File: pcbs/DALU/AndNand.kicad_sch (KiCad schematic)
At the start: 6 parts, among them U501 74HC00, U502 74HC00, U503 74HC14, U504 74HC14, U505 74HC245, U506 74HC245

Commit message: More routing
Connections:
- net A2: now also U501.9; no longer U501.12
- net A3: now also U501.12; no longer U501.9
- net A6: now also U502.9; no longer U502.12
- net A7: now also U502.12; no longer U502.9
- net B2: now also U501.10; no longer U501.13
- net B3: now also U501.13; no longer U501.10
- net B6: now also U502.10; no longer U502.13
- net B7: now also U502.13; no longer U502.10
- net NAND2: now also U501.8; no longer U501.11
- net NAND3: now also U501.11; no longer U501.8
- net NAND6: now also U502.8; no longer U502.11
- net NAND7: now also U502.11; no longer U502.8
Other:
- moved on the sheet: U501C, U501D, U502C, U502D
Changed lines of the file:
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@@
     (pin "7")
   )
-  (symbol (lib_id "74xx:74HC00") (at 83.82 71.12 0) (unit 4)
-    (in_bom yes) (on_board yes) (fields_autoplaced)
-    (property "Reference" "U501" (id 0) (at 83.82 62.23 0))
-    (property "Value" "74HC00" (id 1) (at 83.82 64.77 0))
-    (property "Footprint" "Package_DIP:DIP-14_W7.62mm_Socket" (id 2) (at 83.82 71.12 0)
-      (effects (font (size 1.27 1.27)) hide)
-    )
-    (property "Datasheet" "http://www.ti.com/lit/gpn/sn74hc00" (id 3) (at 83.82 71.12 0)
+  (symbol (lib_id "74xx:74HC00") (at 83.82 85.09 0) (unit 4)
+    (in_bom yes) (on_board yes) (fields_autoplaced)
+    (property "Reference" "U501" (id 0) (at 83.82 76.2 0))
+    (property "Value" "74HC00" (id 1) (at 83.82 78.74 0))
+    (property "Footprint" "Package_DIP:DIP-14_W7.62mm_Socket" (id 2) (at 83.82 85.09 0)
+      (effects (font (size 1.27 1.27)) hide)
+    )
+    (property "Datasheet" "http://www.ti.com/lit/gpn/sn74hc00" (id 3) (at 83.82 85.09 0)
       (effects (font (size 1.27 1.27)) hide)
     )
@@
     (pin "1")
   )
-  (symbol (lib_id "74xx:74HC00") (at 83.82 140.97 0) (unit 3)
-    (in_bom yes) (on_board yes) (fields_autoplaced)
-    (property "Reference" "U502" (id 0) (at 83.82 132.08 0))
-    (property "Value" "74HC00" (id 1) (at 83.82 134.62 0))
-    (property "Footprint" "Package_DIP:DIP-14_W7.62mm_Socket" (id 2) (at 83.82 140.97 0)
-      (effects (font (size 1.27 1.27)) hide)
-    )
-    (property "Datasheet" "http://www.ti.com/lit/gpn/sn74hc00" (id 3) (at 83.82 140.97 0)
+  (symbol (lib_id "74xx:74HC00") (at 83.82 127 0) (unit 3)
+    (in_bom yes) (on_board yes) (fields_autoplaced)
+    (property "Reference" "U502" (id 0) (at 83.82 118.11 0))
+    (property "Value" "74HC00" (id 1) (at 83.82 120.65 0))
+    (property "Footprint" "Package_DIP:DIP-14_W7.62mm_Socket" (id 2) (at 83.82 127 0)
+      (effects (font (size 1.27 1.27)) hide)
+    )
+    (property "Datasheet" "http://www.ti.com/lit/gpn/sn74hc00" (id 3) (at 83.82 127 0)
       (effects (font (size 1.27 1.27)) hide)
     )
@@
     (pin "1")
   )
-  (symbol (lib_id "74xx:74HC00") (at 83.82 85.09 0) (unit 3)
-    (in_bom yes) (on_board yes) (fields_autoplaced)
-    (property "Reference" "U501" (id 0) (at 83.82 76.2 0))
-    (property "Value" "74HC00" (id 1) (at 83.82 78.74 0))
-    (property "Footprint" "Package_DIP:DIP-14_W7.62mm_Socket" (id 2) (at 83.82 85.09 0)
-      (effects (font (size 1.27 1.27)) hide)
-    )
-    (property "Datasheet" "http://www.ti.com/lit/gpn/sn74hc00" (id 3) (at 83.82 85.09 0)
+  (symbol (lib_id "74xx:74HC00") (at 83.82 71.12 0) (unit 3)
+    (in_bom yes) (on_board yes) (fields_autoplaced)
+    (property "Reference" "U501" (id 0) (at 83.82 62.23 0))
+    (property "Value" "74HC00" (id 1) (at 83.82 64.77 0))
+    (property "Footprint" "Package_DIP:DIP-14_W7.62mm_Socket" (id 2) (at 83.82 71.12 0)
+      (effects (font (size 1.27 1.27)) hide)
+    )
+    (property "Datasheet" "http://www.ti.com/lit/gpn/sn74hc00" (id 3) (at 83.82 71.12 0)
       (effects (font (size 1.27 1.27)) hide)
     )
@@
     (pin "7")
   )
-  (symbol (lib_id "74xx:74HC00") (at 83.82 127 0) (unit 4)
-    (in_bom yes) (on_board yes) (fields_autoplaced)
-    (property "Reference" "U502" (id 0) (at 83.82 118.11 0))
-    (property "Value" "74HC00" (id 1) (at 83.82 120.65 0))
-    (property "Footprint" "Package_DIP:DIP-14_W7.62mm_Socket" (id 2) (at 83.82 127 0)
-      (effects (font (size 1.27 1.27)) hide)
-    )
-    (property "Datasheet" "http://www.ti.com/lit/gpn/sn74hc00" (id 3) (at 83.82 127 0)
-      (effects (font (size 1.27 1.27)) hide)
-    )
+  (symbol (lib_id "74xx:74HC00") (at 83.82 140.97 0) (unit 4)
+    (in_bom yes) (on_board yes) (fields_autoplaced)
+    (property "Reference" "U502" (id 0) (at 83.82 132.08 0))
+    (property "Value" "74HC00" (id 1) (at 83.82 134.62 0))
+    (property "Footprint" "Package_DIP:DIP-14_W7.62mm_Socket" (id 2) (at 83.82 140.97 0)
+      (effects (font (size 1.27 1.27)) hide)
+    )
+    (property "Datasheet" "http://www.ti.com/lit/gpn/sn74hc00" (id 3) (at 83.82 140.97 0)
+      (effects (font (size 1.27 1.27)) hide)
+    )

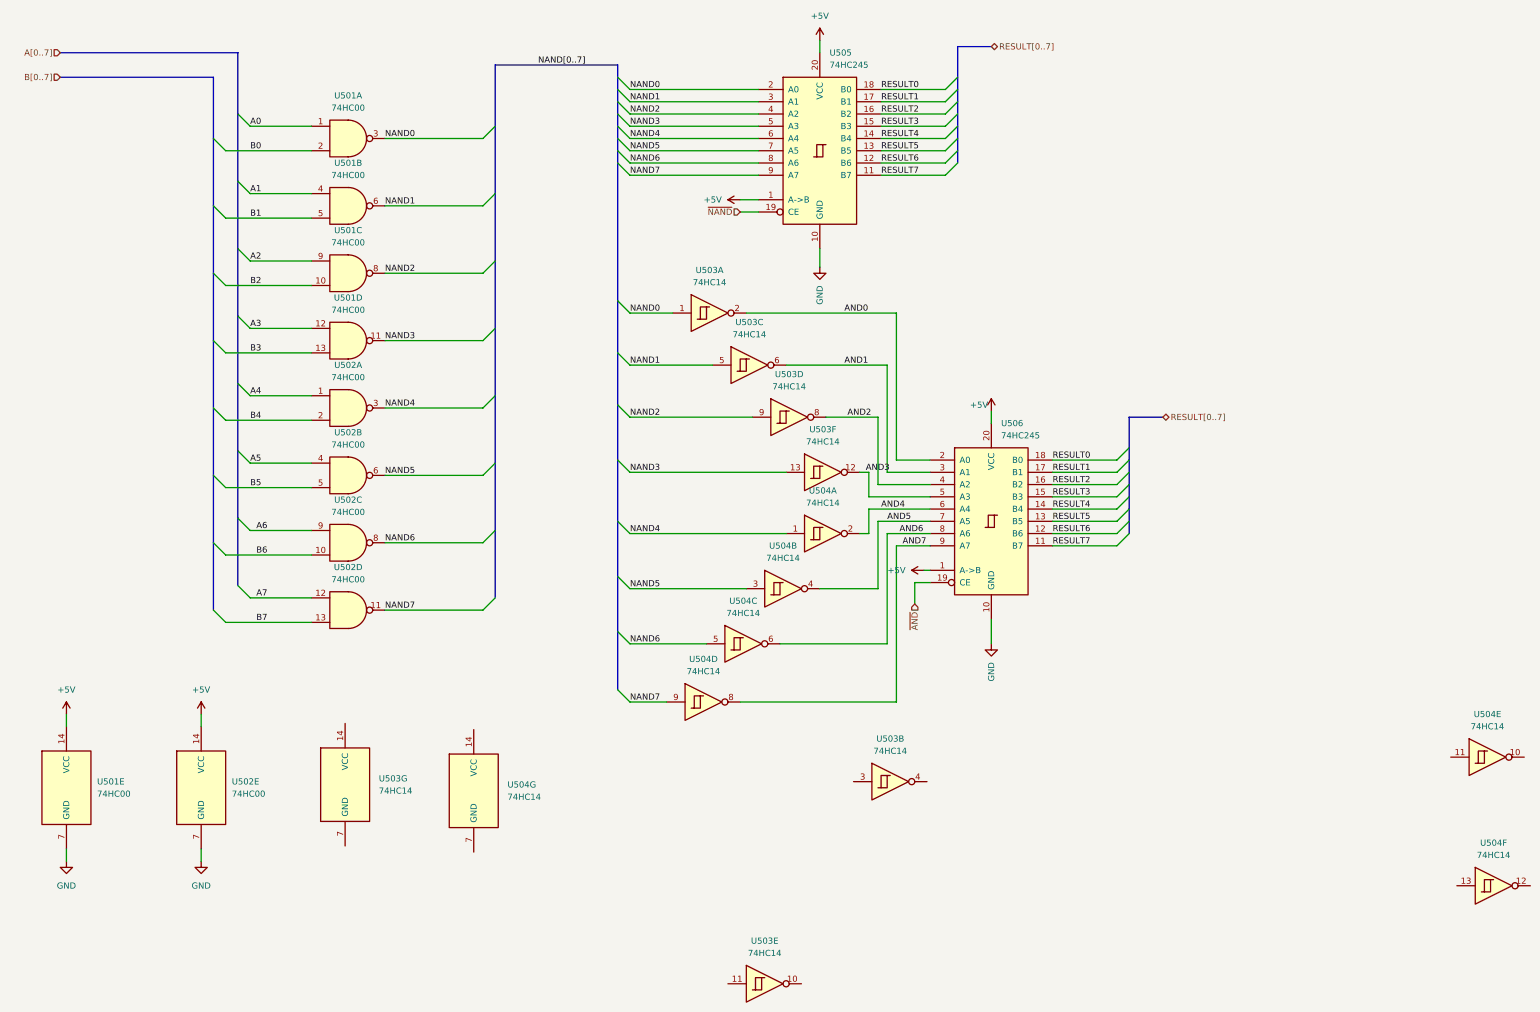
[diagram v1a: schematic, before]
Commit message: Removing diode ORs (mainly). Preparing for a small rethink
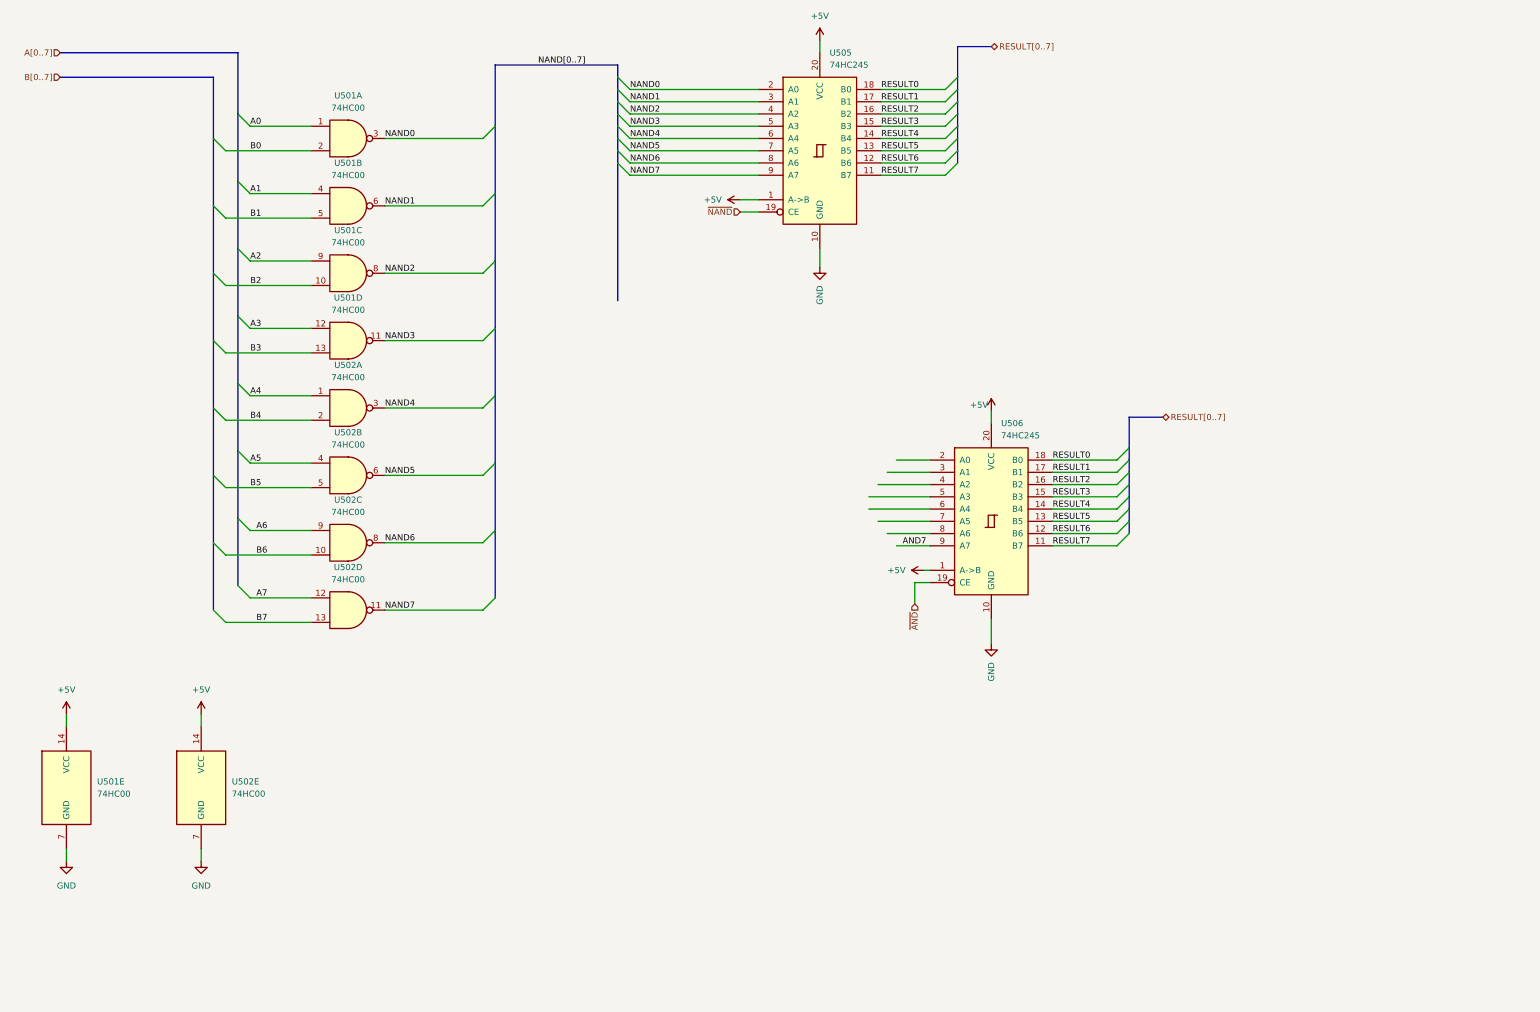
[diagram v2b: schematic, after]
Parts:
- removed U503, U504: 74HC14, Package_SO:SOIC-14_3.9x8.7mm_P1.27mm, symbol 74xx:74HC14
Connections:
- net AND0: no longer names the net of U506.2 (A0)
- net AND1: no longer names the net of U506.3 (A1)
- net AND2: no longer names the net of U506.4 (A2)
- net AND3: no longer names the net of U506.5 (A3)
- net AND4: no longer names the net of U506.6 (A4)
- net AND5: no longer names the net of U506.7 (A5)
- net AND6: no longer names the net of U506.8 (A6)

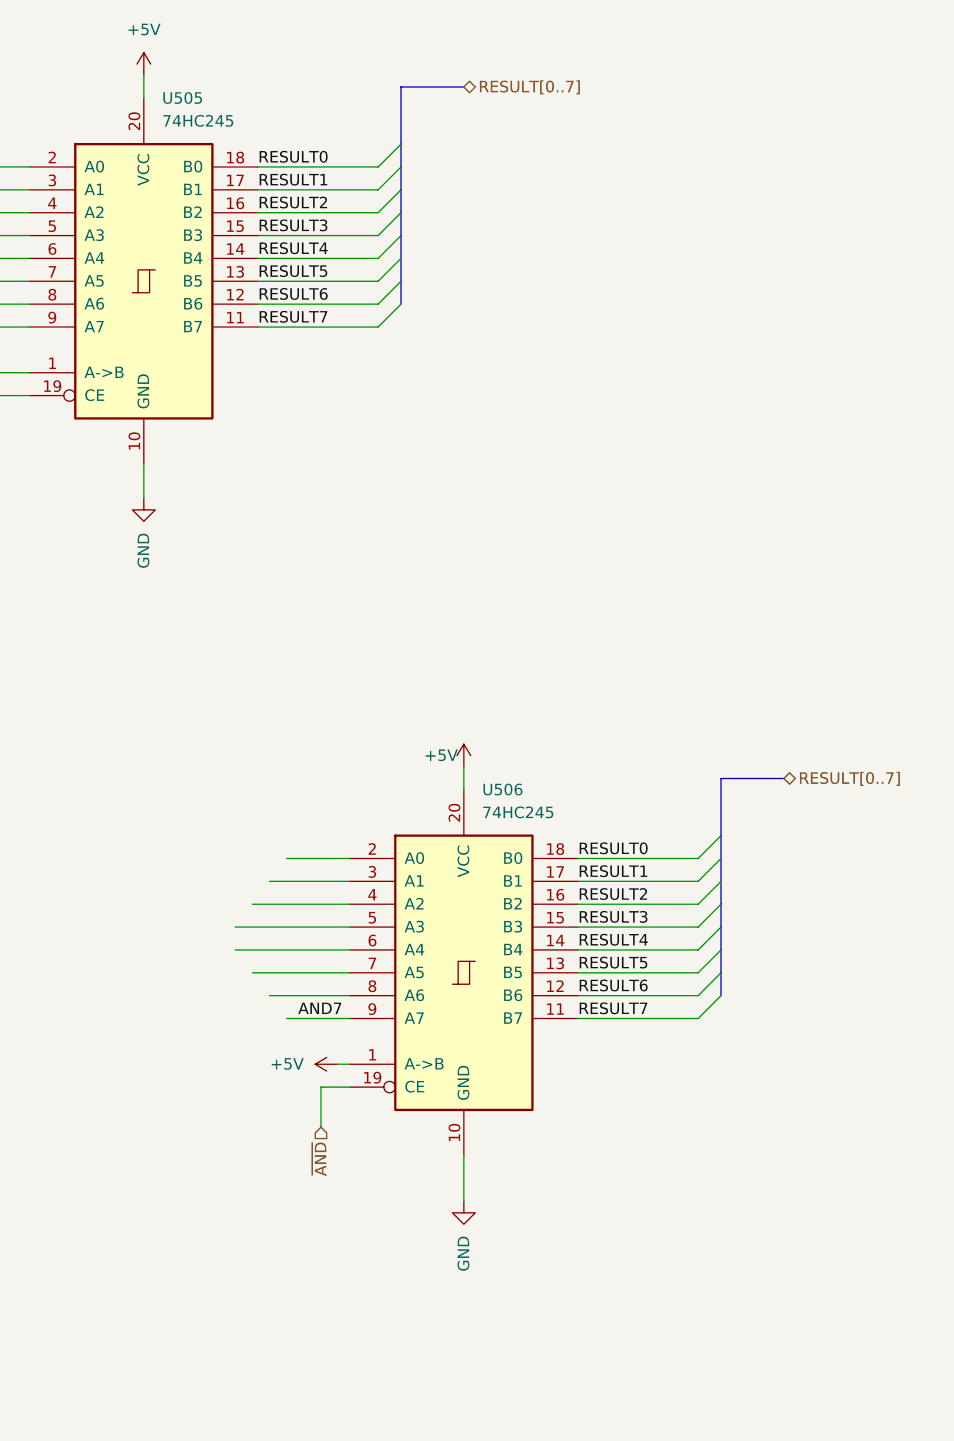
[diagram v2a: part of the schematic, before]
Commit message: Separate out AND stage
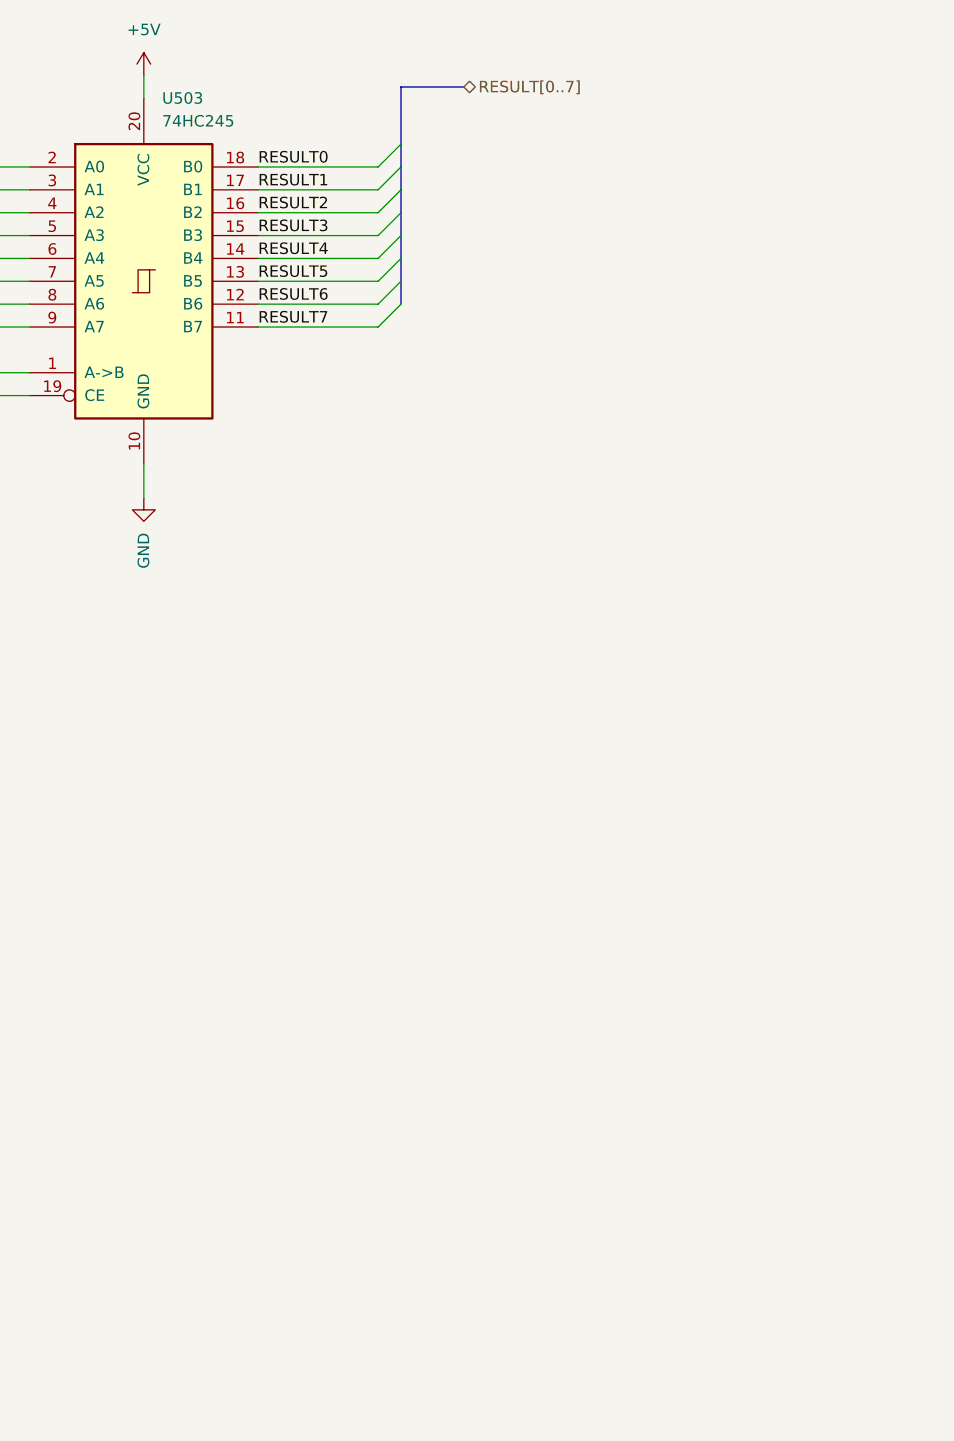
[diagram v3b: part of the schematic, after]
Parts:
- removed U506: 74HC245, Package_SO:SOIC-20W_7.5x12.8mm_P1.27mm, symbol 74xx:74HC245
- renumbered U505 to U503

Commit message: Fixing a lot of routing
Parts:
- added C501, C502, C503: 100n, Capacitor_SMD:C_0603_1608Metric, symbol Device:C
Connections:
- net +5V: now also C501.1, C502.1, C503.1
- net A0: now also U501.9; no longer U501.1
- net A1: now also U501.12; no longer U501.4
- net A2: now also U501.1; no longer U501.9
- net A3: now also U501.4; no longer U501.12
- net B0: now also U501.10; no longer U501.2
- net B1: now also U501.13; no longer U501.5
- net B2: now also U501.2; no longer U501.10
- net B3: now also U501.5; no longer U501.13
- net GND: now also C501.2, C502.2, C503.2
- net NAND0: now also U501.8; no longer U501.3
- net NAND1: now also U501.11; no longer U501.6
- net NAND2: now also U501.3; no longer U501.8
- net NAND3: now also U501.6; no longer U501.11
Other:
- moved on the sheet: U501A, U501B, U501C, U501D

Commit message: Sending for production
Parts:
- U501, U502: now left out of the parts list
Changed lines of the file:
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@@
   )
   (symbol (lib_id "74xx:74HC00") (at 83.82 113.03 0) (unit 2)
-    (in_bom yes) (on_board yes)
+    (in_bom no) (on_board yes)
     (property "Reference" "U502" (id 0) (at 83.82 104.14 0))
     (property "Value" "74HC00" (id 1) (at 83.82 106.68 0))
@@
   )
   (symbol (lib_id "74xx:74HC00") (at 83.82 57.15 0) (unit 4)
-    (in_bom yes) (on_board yes) (fields_autoplaced)
+    (in_bom no) (on_board yes) (fields_autoplaced)
     (property "Reference" "U501" (id 0) (at 83.82 48.26 0))
     (property "Value" "74HC00" (id 1) (at 83.82 50.8 0))
@@
   )
   (symbol (lib_id "74xx:74HC00") (at 83.82 127 0) (unit 3)
-    (in_bom yes) (on_board yes) (fields_autoplaced)
+    (in_bom no) (on_board yes) (fields_autoplaced)
     (property "Reference" "U502" (id 0) (at 83.82 118.11 0))
     (property "Value" "74HC00" (id 1) (at 83.82 120.65 0))
@@
   )
   (symbol (lib_id "74xx:74HC00") (at 83.82 71.12 0) (unit 1)
-    (in_bom yes) (on_board yes) (fields_autoplaced)
+    (in_bom no) (on_board yes) (fields_autoplaced)
     (property "Reference" "U501" (id 0) (at 83.82 62.23 0))
     (property "Value" "74HC00" (id 1) (at 83.82 64.77 0))
@@
   )
   (symbol (lib_id "74xx:74HC00") (at 83.82 43.18 0) (unit 3)
-    (in_bom yes) (on_board yes) (fields_autoplaced)
+    (in_bom no) (on_board yes) (fields_autoplaced)
     (property "Reference" "U501" (id 0) (at 83.82 34.29 0))
     (property "Value" "74HC00" (id 1) (at 83.82 36.83 0))
@@
   )
   (symbol (lib_id "74xx:74HC00") (at 83.82 99.06 0) (unit 1)
-    (in_bom yes) (on_board yes) (fields_autoplaced)
+    (in_bom no) (on_board yes) (fields_autoplaced)
     (property "Reference" "U502" (id 0) (at 83.82 90.17 0))
     (property "Value" "74HC00" (id 1) (at 83.82 92.71 0))
@@
   )
   (symbol (lib_id "74xx:74HC00") (at 83.82 140.97 0) (unit 4)
-    (in_bom yes) (on_board yes) (fields_autoplaced)
+    (in_bom no) (on_board yes) (fields_autoplaced)
     (property "Reference" "U502" (id 0) (at 83.82 132.08 0))
     (property "Value" "74HC00" (id 1) (at 83.82 134.62 0))
@@
   )
   (symbol (lib_id "74xx:74HC00") (at 83.82 85.09 0) (unit 2)
-    (in_bom yes) (on_board yes) (fields_autoplaced)
+    (in_bom no) (on_board yes) (fields_autoplaced)
     (property "Reference" "U501" (id 0) (at 83.82 76.2 0))
     (property "Value" "74HC00" (id 1) (at 83.82 78.74 0))
@@
   )
   (symbol (lib_id "74xx:74HC00") (at 53.34 177.8 0) (unit 5)
-    (in_bom yes) (on_board yes) (fields_autoplaced)
+    (in_bom no) (on_board yes) (fields_autoplaced)
     (property "Reference" "U502" (id 0) (at 59.69 176.5299 0)
       (effects (font (size 1.27 1.27)) (justify left))
@@
   )
   (symbol (lib_id "74xx:74HC00") (at 25.4 177.8 0) (unit 5)
-    (in_bom yes) (on_board yes) (fields_autoplaced)
+    (in_bom no) (on_board yes) (fields_autoplaced)
     (property "Reference" "U501" (id 0) (at 31.75 176.5299 0)
       (effects (font (size 1.27 1.27)) (justify left))
